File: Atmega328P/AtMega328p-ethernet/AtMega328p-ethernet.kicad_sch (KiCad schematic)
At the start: 20 parts, among them J1 Conn_01x05_Socket, J4 Conn_01x06_Socket, J5 Conn_01x06_Socket, J6 Conn_01x06_Socket, J7 Conn_01x06_Socket, J8 Conn_02x03_Counter_Clockwise, SW1 SW_Push, U1 ATmega328P-A, Y1 16MHz

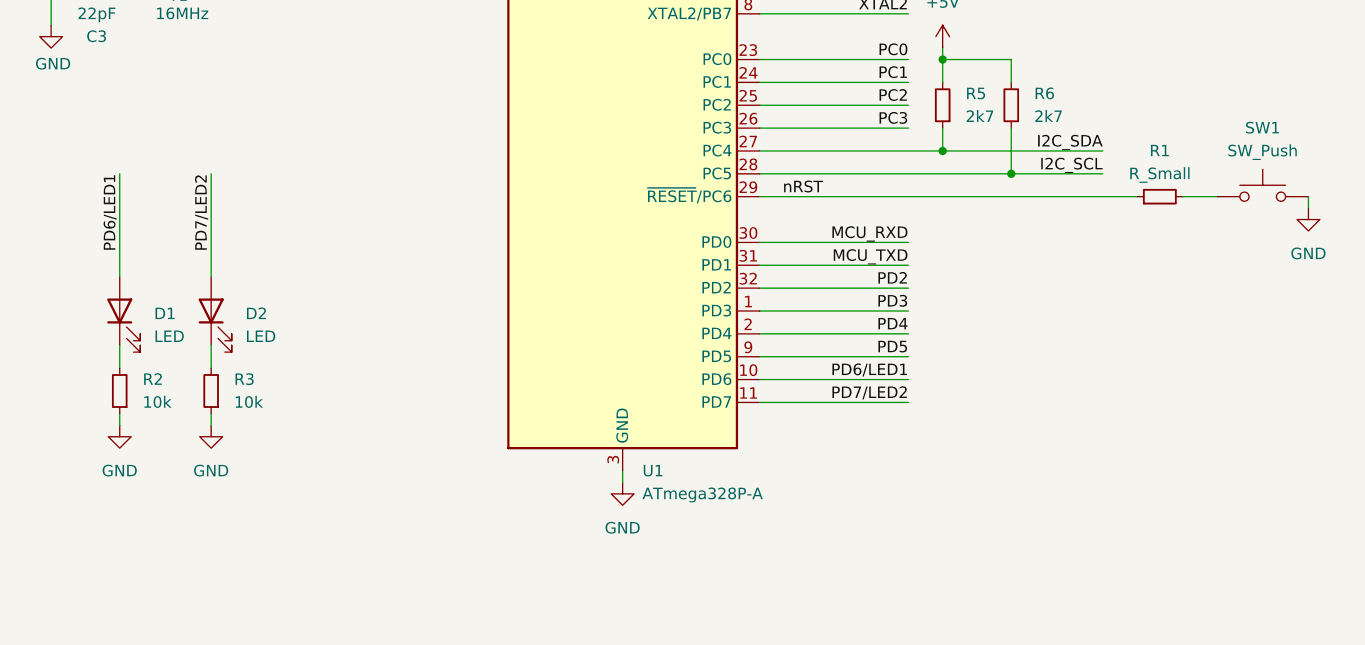
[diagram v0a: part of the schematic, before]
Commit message: Most components selected using lcsc
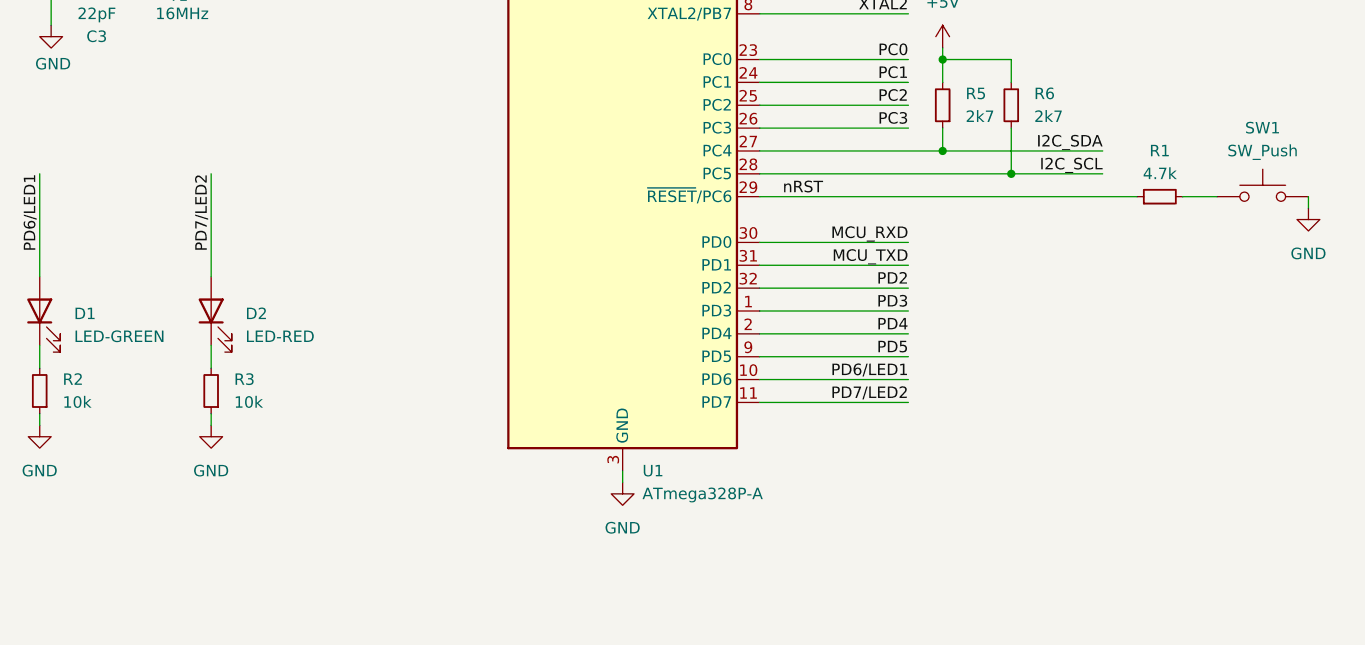
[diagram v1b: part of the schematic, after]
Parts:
- C2: footprint Capacitor_SMD:CP_Elec_4x3 -> Capacitor_SMD:C_1206_3216Metric
- D1: value LED -> LED-GREEN; footprint LED_SMD:LED_0603_1608Metric -> LED_SMD:LED_0805_2012Metric
- D2: value LED -> LED-RED; footprint LED_SMD:LED_0603_1608Metric -> LED_SMD:LED_0805_2012Metric
- J1, J4, J5, J6, J7, J8: now left out of the parts list
- R1: value R_Small -> 4.7k; LCSC (none) -> C23162
- SW1: footprint Button_Switch_SMD:SW_Push_1P1T_NO_CK_KMR2 -> Button_Switch_SMD:SW_Push_1P1T_XKB_TS-1187A; LCSC (none) -> C318884
- U1: LCSC (none) -> C14877
- Y1: footprint Crystal:Crystal_SMD_2012-2Pin_2.0x1.2mm -> Crystal:Crystal_SMD_3225-4Pin_3.2x2.5mm
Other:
- moved on the sheet: D1, R2
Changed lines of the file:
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@@
 	(wire
 		(pts
-			(xy 67.31 100.33) (xy 67.31 111.76)
+			(xy 58.42 100.33) (xy 58.42 111.76)
 		)
 		(stroke
@@
 	(wire
 		(pts
-			(xy 67.31 127) (xy 67.31 128.27)
+			(xy 58.42 127) (xy 58.42 128.27)
 		)
 		(stroke
@@
 	(wire
 		(pts
-			(xy 67.31 119.38) (xy 67.31 121.92)
+			(xy 58.42 119.38) (xy 58.42 121.92)
 		)
 		(stroke
@@
 	)
 	(label "PD6{slash}LED1"
-		(at 67.31 100.33 270)
+		(at 58.42 100.33 270)
 		(effects
 			(font
@@
 	(symbol
 		(lib_id "power:GND")
-		(at 67.31 128.27 0)
+		(at 58.42 128.27 0)
 		(unit 1)
 		(exclude_from_sim no)
@@
 		(fields_autoplaced yes)
 		(property "Reference" "#PWR01"
-			(at 67.31 134.62 0)
+			(at 58.42 134.62 0)
 			(effects
 				(font
@@
 		)
 		(property "Value" "GND"
-			(at 67.31 133.35 0)
+			(at 58.42 133.35 0)
 			(effects
 				(font
@@
 		)
 		(property "Footprint" ""
-			(at 67.31 128.27 0)
+			(at 58.42 128.27 0)
 			(effects
 				(font
@@
 		)
 		(property "Datasheet" ""
-			(at 67.31 128.27 0)
+			(at 58.42 128.27 0)
 			(effects
 				(font
@@
 		)
 		(property "Description" "Power symbol creates a global label with name \"GND\" , ground"
-			(at 67.31 128.27 0)
+			(at 58.42 128.27 0)
 			(effects
 				(font
@@
 			)
 		)
-		(property "Footprint" "Button_Switch_SMD:SW_Push_1P1T_NO_CK_KMR2"
+		(property "Footprint" "Button_Switch_SMD:SW_Push_1P1T_XKB_TS-1187A"
 			(at 194.31 97.79 0)
 			(effects
@@
 			)
 		)
+		(property "LCSC" "C318884"
+			(at 194.31 102.87 0)
+			(effects
+				(font
+					(size 1.27 1.27)
+				)
+				(hide yes)
+			)
+		)
 		(pin "1"
 		)
@@
 			)
 		)
+		(property "LCSC" "C14877"
+			(at 123.19 95.25 0)
+			(effects
+				(font
+					(size 1.27 1.27)
+				)
+				(hide yes)
+			)
+		)
 		(pin "13"
 		)
@@
 		(unit 1)
 		(exclude_from_sim no)
-		(in_bom yes)
+		(in_bom no)
 		(on_board yes)
 		(dnp no)
@@
 		(unit 1)
 		(exclude_from_sim no)
-		(in_bom yes)
+		(in_bom no)
 		(on_board yes)
 		(dnp no)
@@
 			)
 		)
-		(property "Value" "R_Small"
+		(property "Value" "4.7k"
 			(at 182.88 100.33 90)
 			(effects
@@
 			)
 		)
+		(property "LCSC" "C23162"
+			(at 182.88 102.87 0)
+			(effects
+				(font
+					(size 1.27 1.27)
+				)
+				(hide yes)
+			)
+		)
 		(pin "1"
 		)
@@
 		(unit 1)
 		(exclude_from_sim no)
-		(in_bom yes)
+		(in_bom no)
 		(on_board yes)
 		(dnp no)
@@
 		(unit 1)
 		(exclude_from_sim no)
-		(in_bom yes)
+		(in_bom no)
 		(on_board yes)
 		(dnp no)
@@
 		(unit 1)
 		(exclude_from_sim no)
-		(in_bom yes)
+		(in_bom no)
 		(on_board yes)
 		(dnp no)
@@
 	(symbol
 		(lib_id "Device:R_Small")
-		(at 67.31 124.46 180)
+		(at 58.42 124.46 180)
 		(unit 1)
 		(exclude_from_sim no)
@@
 		(fields_autoplaced yes)
 		(property "Reference" "R2"
-			(at 69.85 123.1899 0)
+			(at 60.96 123.1899 0)
 			(effects
 				(font
@@
 		)
 		(property "Value" "10k"
-			(at 69.85 125.7299 0)
+			(at 60.96 125.7299 0)
 			(effects
 				(font
@@
 		)
 		(property "Footprint" "Resistor_SMD:R_0603_1608Metric"
-			(at 67.31 124.46 0)
+			(at 58.42 124.46 0)
 			(effects
 				(font
@@
 		)
 		(property "Datasheet" "~"
-			(at 67.31 124.46 0)
+			(at 58.42 124.46 0)
 			(effects
 				(font
@@
 		)
 		(property "Description" "Resistor, small symbol"
-			(at 67.31 124.46 0)
+			(at 58.42 124.46 0)
 			(effects
 				(font
@@
 		)
 		(property "LCSC" "C25804"
-			(at 67.31 124.46 0)
+			(at 58.42 124.46 0)
 			(effects
 				(font
@@
 			)
 		)
-		(property "Footprint" "Crystal:Crystal_SMD_2012-2Pin_2.0x1.2mm"
+		(property "Footprint" "Crystal:Crystal_SMD_3225-4Pin_3.2x2.5mm"
 			(at 73.66 74.93 0)
 			(effects
@@
 		(unit 1)
 		(exclude_from_sim no)
-		(in_bom yes)
+		(in_bom no)
 		(on_board yes)
 		(dnp no)
@@
 			)
 		)
-		(property "Value" "LED"
+		(property "Value" "LED-RED"
 			(at 81.28 118.4274 90)
 			(effects
@@
 			)
 		)
-		(property "Footprint" "LED_SMD:LED_0603_1608Metric"
+		(property "Footprint" "LED_SMD:LED_0805_2012Metric"
 			(at 77.47 115.57 0)
 			(effects
@@
 	(symbol
 		(lib_id "Device:LED")
-		(at 67.31 115.57 90)
+		(at 58.42 115.57 90)
 		(unit 1)
 		(exclude_from_sim no)
@@
 		(fields_autoplaced yes)
 		(property "Reference" "D1"
-			(at 71.12 115.8874 90)
+			(at 62.23 115.8874 90)
 			(effects
 				(font
@@
 			)
 		)
-		(property "Value" "LED"
-			(at 71.12 118.4274 90)
+		(property "Value" "LED-GREEN"
+			(at 62.23 118.4274 90)
 			(effects
 				(font
@@
 			)
 		)
-		(property "Footprint" "LED_SMD:LED_0603_1608Metric"
-			(at 67.31 115.57 0)
+		(property "Footprint" "LED_SMD:LED_0805_2012Metric"
+			(at 58.42 115.57 0)
 			(effects
 				(font
@@
 		)
 		(property "Datasheet" "~"
-			(at 67.31 115.57 0)
+			(at 58.42 115.57 0)
 			(effects
 				(font
@@
 		)
 		(property "Description" "Light emitting diode"
-			(at 67.31 115.57 0)
+			(at 58.42 115.57 0)
 			(effects
 				(font
@@
 		)
 		(property "LCSC" "C2297"
-			(at 67.31 115.57 0)
+			(at 58.42 115.57 0)
 			(effects
 				(font
@@
 			)
 		)
-		(property "Footprint" "Capacitor_SMD:CP_Elec_4x3"
+		(property "Footprint" "Capacitor_SMD:C_1206_3216Metric"
 			(at 101.6 52.07 0)
 			(effects

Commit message: Continued cleanup
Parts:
- removed J1: Conn_01x05_Socket, Connector_PinHeader_2.54mm:PinHeader_1x05_P2.54mm_Vertical, symbol Connector:Conn_01x05_Socket
- added C26: 100nF, Capacitor_SMD:C_0603_1608Metric, symbol Device:C_Small
- added FB1, FB2: 100R@100MHz, Inductor_SMD:L_0603_1608Metric, symbol Device:FerriteBead_Small
- added J1: Conn_01x06_Socket, Connector_PinHeader_2.54mm:PinHeader_1x06_P2.54mm_Vertical, symbol Connector:Conn_01x06_Socket
- Y1: symbol Device:Crystal -> Device:Crystal_GND24
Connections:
- net ETH_SPI_SS is gone; now on net GND: U1.14 (PB2)
- net +5V: now also C26.1, FB2.2, J1.1 (Pin_1)
- net GND: now also C26.2, J1.2 (Pin_2), J1.6 (Pin_6)
- net SPI_MISO: now also J1.4 (Pin_4)
- net SPI_MOSI: now also J1.5 (Pin_5)
- net SPI_SCK: now also J1.3 (Pin_3)
- net XTAL2: now also Y1.3; no longer Y1.2
- new net +3.3V: FB1.2
- new net ETHERNET_MODULE/+3.3VA_IN: FB1.1
- new net VBUS: FB2.1
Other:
- sheet ETHERNET_MODULE ports: added +3.3VA_IN, +3.3V_IN; removed none
- sheet POWER SUPPLIES ports: added +3.3V_OUT, +5V_IN; removed none
- sheet USB_INTERFACE ports: added VBUS_OUT; removed none
- note added: "Reference Design recommends HH-1M1608-121JT"

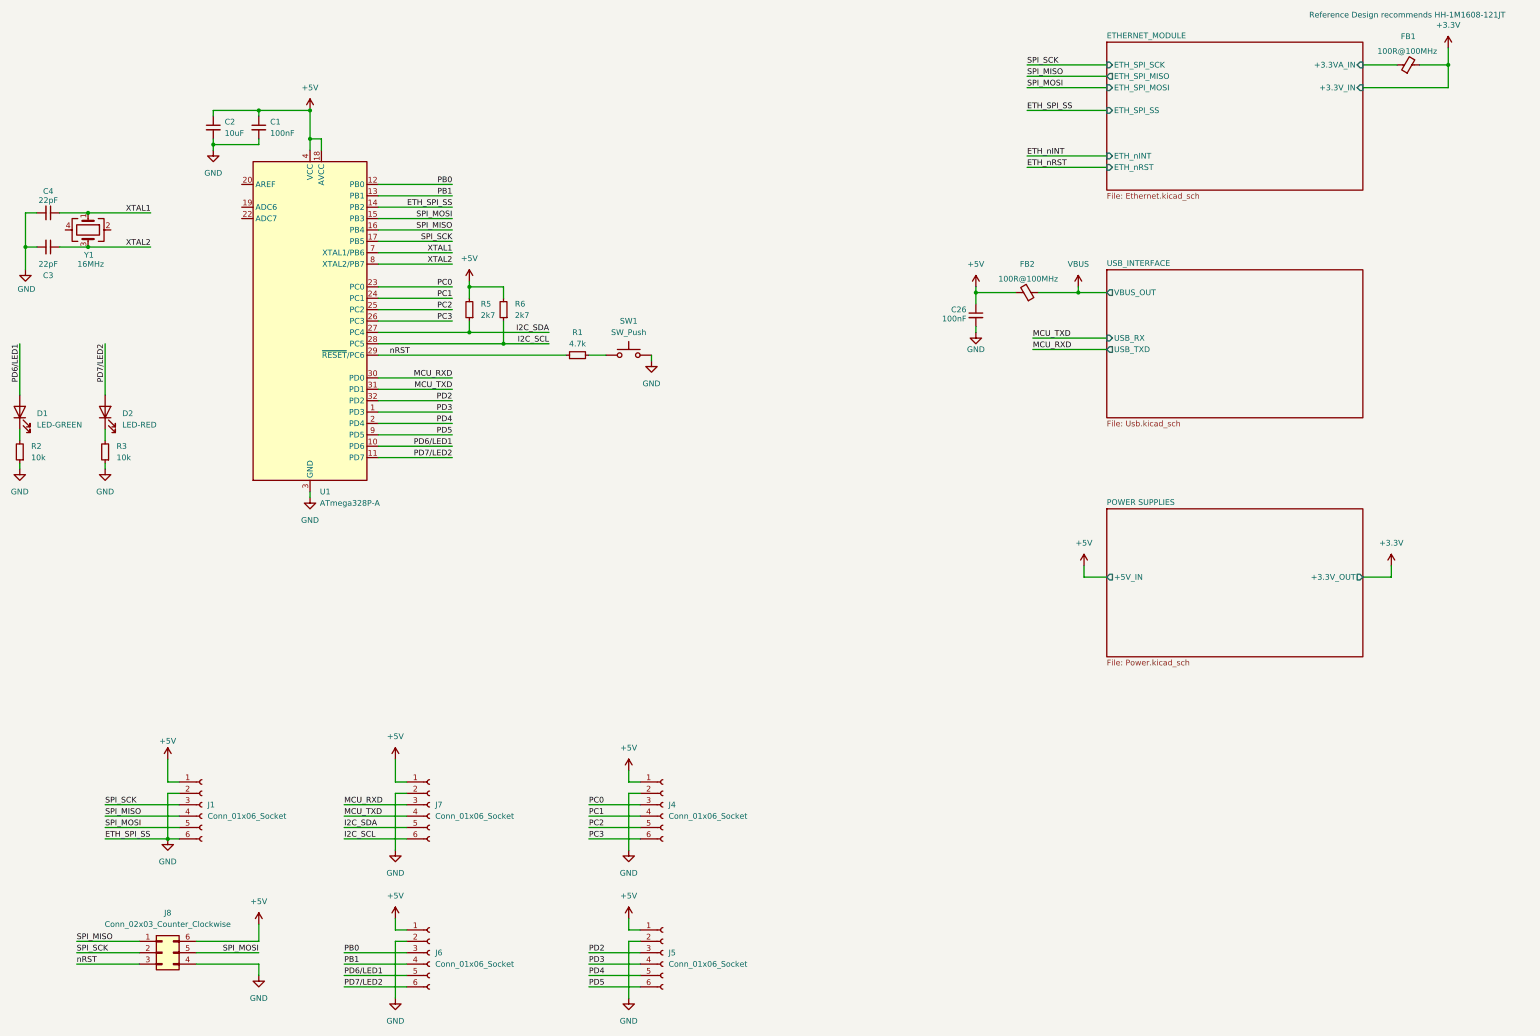
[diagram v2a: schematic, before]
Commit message: Most components layed out and locked still to do ethernet
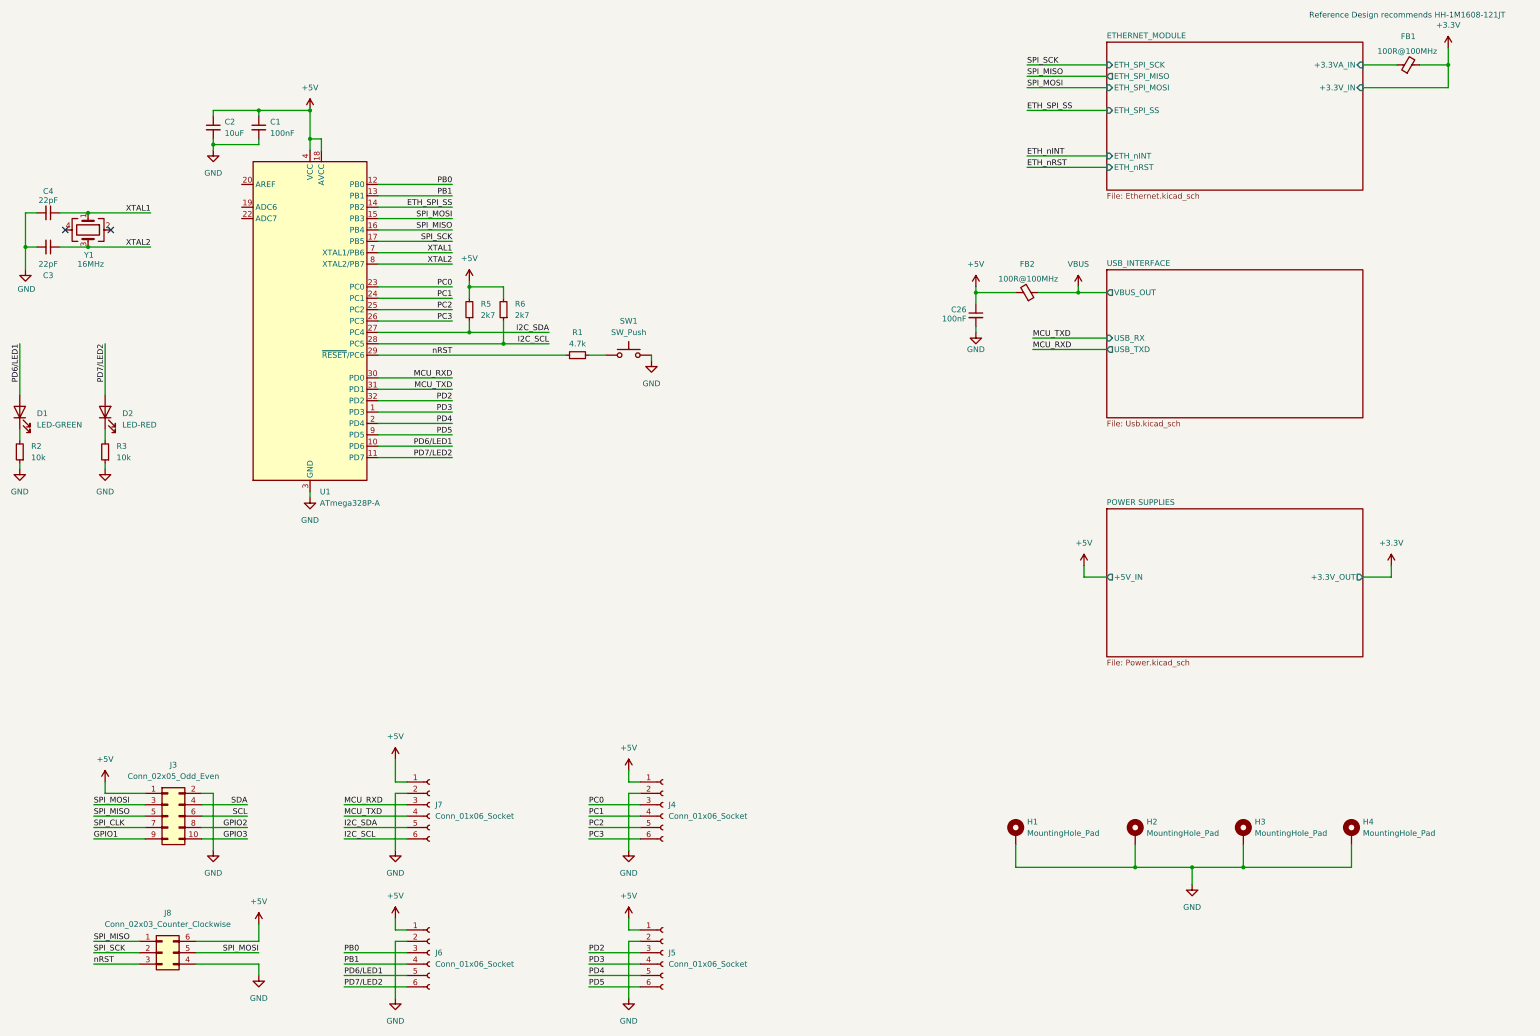
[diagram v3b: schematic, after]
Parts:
- removed J1: Conn_01x06_Socket, Connector_PinHeader_2.54mm:PinHeader_1x06_P2.54mm_Vertical, symbol Connector:Conn_01x06_Socket
- added H1, H2, H3, H4: MountingHole_Pad, MountingHole:MountingHole_3.2mm_M3_DIN965_Pad, symbol Mechanical:MountingHole_Pad
- added J3: Conn_02x05_Odd_Even, Connector_IDC:IDC-Header_2x05_P2.54mm_Horizontal, symbol Connector_Generic:Conn_02x05_Odd_Even
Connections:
- net +5V: now also J3.1 (Pin_1)
- net GND: now also H1.1, H2.1, H3.1, H4.1, J3.2 (Pin_2); no longer U1.14 (PB2)
- net SPI_MISO: now also J3.5 (Pin_5)
- net SPI_MOSI: now also J3.3 (Pin_3)
- new net ETH_SPI_SS: U1.14 (PB2)
- new net GPIO1: J3.9 (Pin_9)
- new net GPIO2: J3.8 (Pin_8)
- new net GPIO3: J3.10 (Pin_10)
- new net SCL: J3.6 (Pin_6)
- new net SDA: J3.4 (Pin_4)
- new net SPI_CLK: J3.7 (Pin_7)
- no-connect marks 0 -> 2

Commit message: Layout complete ready for review
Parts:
- added J10: Conn_02x03_Counter_Clockwise, Connector_PinHeader_2.54mm:PinHeader_2x03_P2.54mm_Vertical, symbol Connector_Generic:Conn_02x03_Odd_Even
- J8: symbol Connector_Generic:Conn_02x03_Counter_Clockwise -> Connector_Generic:Conn_02x03_Odd_Even; now in the parts list
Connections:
- net GPIO2 is gone; now on net PD5: J3.8 (Pin_8)
- net GPIO3 is gone; now on net PC0: J3.10 (Pin_10)
- net +3.3V: now also J4.1 (Pin_1), J7.1 (Pin_1)
- net +5V: now also J8.2 (Pin_2); no longer J4.1 (Pin_1), J7.1 (Pin_1), J8.6 (Pin_6)
- net ETH_SPI_SS: now also J10.2 (Pin_2); no longer U1.14 (PB2)
- net ETH_nINT: now also J10.4 (Pin_4)
- net ETH_nRST: now also J10.6 (Pin_6)
- net GND: now also J8.6 (Pin_6); no longer J8.4 (Pin_4)
- net PC0: now also J10.3 (Pin_3)
- net PD5: now also J10.5 (Pin_5)
- net SPI_MOSI: now also J8.4 (Pin_4); no longer J8.5 (Pin_5)
- net SPI_SCK: now also J8.3 (Pin_3); no longer J8.2 (Pin_2)
- net nRST: now also J8.5 (Pin_5); no longer J8.3 (Pin_3)
- net GPIO1 renamed PB2
- net PB2: now also U1.14 (PB2), J10.1 (Pin_1)
